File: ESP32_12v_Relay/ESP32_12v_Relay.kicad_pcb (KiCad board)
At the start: 4 copper layers, 54.1 x 54.1 mm, 49 parts, among them IC1 DMN2029USD-13, IC2 DMN2029USD-13, J1 691137710002, J2 691137710002, J3 691137710002, J4 691137710002, J5 Conn_01x06_Female, J6 691137710002, U1 ESP32-C3-WROOM-02-H4, U2 AP6502SP-13

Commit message: Cleaned up projects
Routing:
- net +12V: vias 31 -> 32

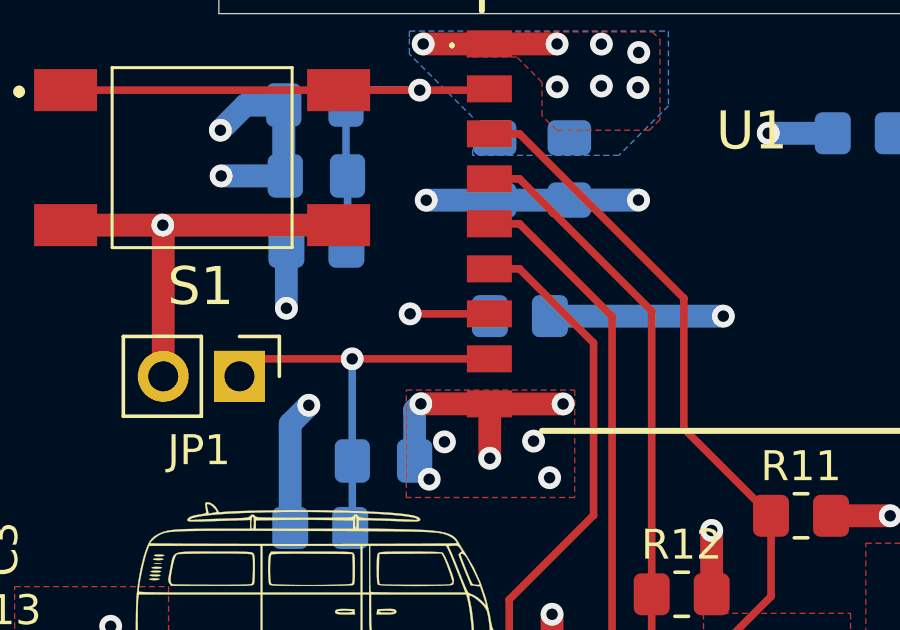
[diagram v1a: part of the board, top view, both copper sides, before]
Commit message: Fixed missing connection in PCB file
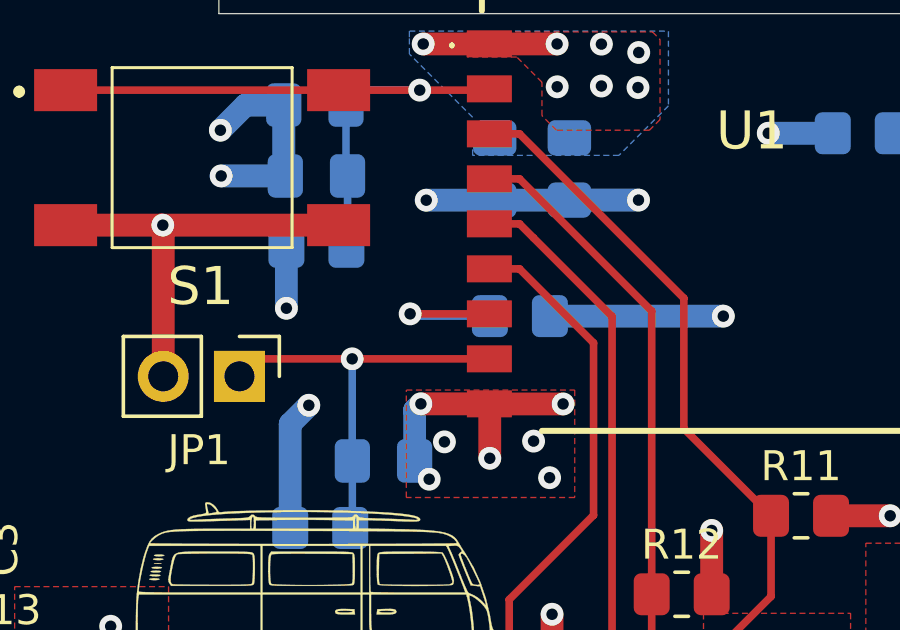
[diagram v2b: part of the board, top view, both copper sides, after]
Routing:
- net /GPIO8: track 2.64 -> 5.33 mm
